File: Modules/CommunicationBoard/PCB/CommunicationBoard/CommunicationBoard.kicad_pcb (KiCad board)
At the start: 2 copper layers, 50 x 60 mm, 12 parts, among them J1 CIO_MAIN_CONNECTOR, J2 Conn_Coaxial, U1 SX1278

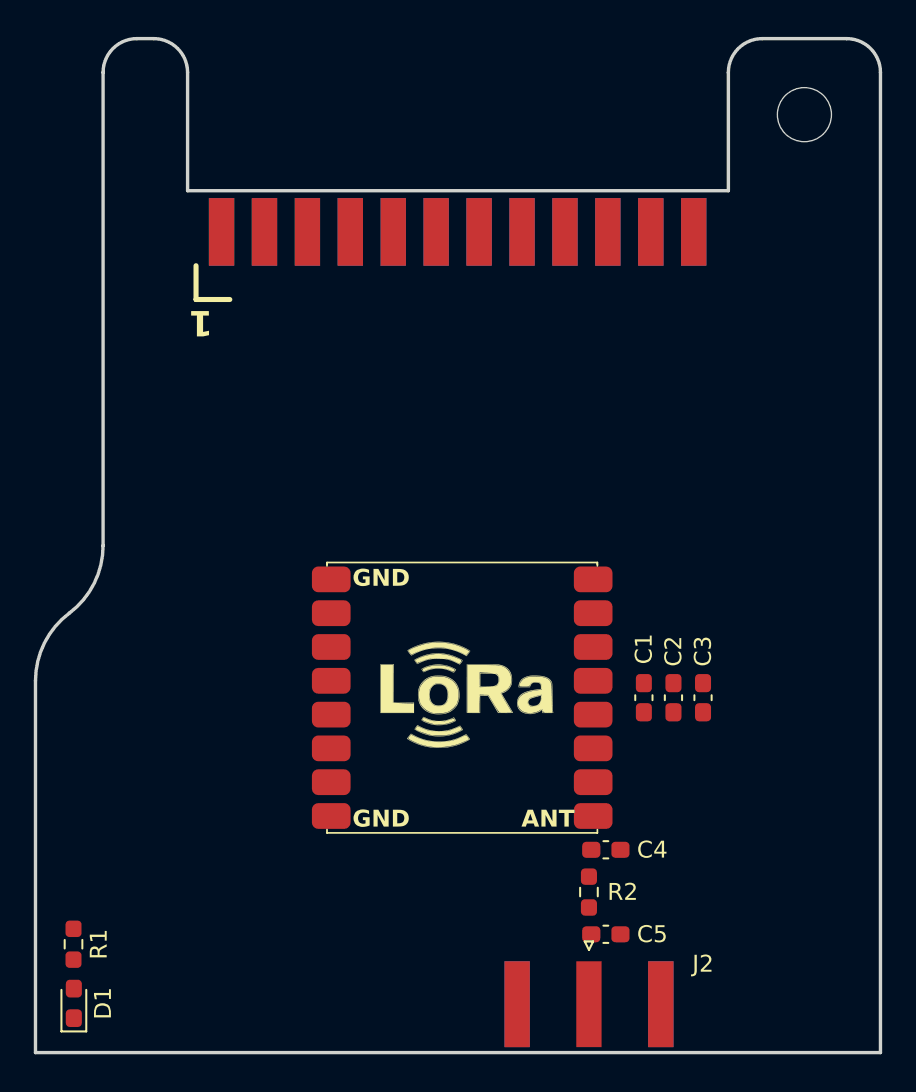
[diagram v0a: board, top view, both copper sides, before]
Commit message: Update Communication Board with E22-900M30S module
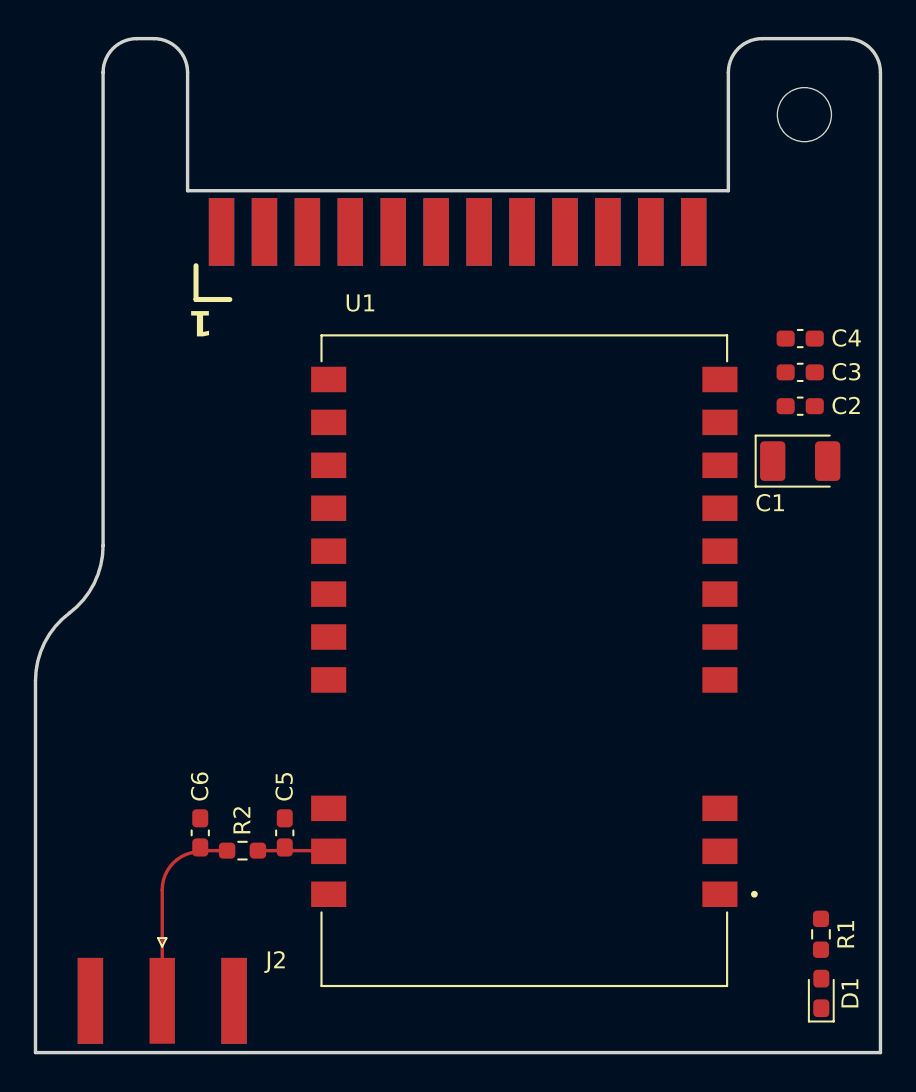
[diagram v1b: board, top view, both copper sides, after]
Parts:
- added C6: NC, Capacitor_SMD:C_0603_1608Metric_Pad1.08x0.95mm_HandSolder, F.Cu at (134.8, 112.0)
- C1: value 10uF -> 220u; footprint Capacitor_SMD:C_0603_1608Metric_Pad1.08x0.95mm_HandSolder -> Capacitor_Tantalum_SMD:CP_EIA-3528-21_Kemet-B_Pad1.50x2.35mm_HandSolder
- C2: value 0.1uF -> 10uF
- C4: value NC -> 0.1uF
- U1: value SX1278 -> E22-900M30S; footprint IcaroFootprints:SX1278 MODULE -> IcaroFootprints:XCVR_E22-900M30S
- moved D1 44.2 mm to (171.5, 121.5)
- moved R1 44.2 mm to (171.5, 118.0)
- moved C4 32.4 mm to (170.2, 82.8)
- moved J2 25.3 mm to (132.5, 121.9)
- moved R2 20.6 mm to (137.2, 113.0), turned to 180 degrees
- moved C3 20.1 mm to (170.2, 84.8), turned to 0 degrees
- moved C5 19.9 mm to (139.8, 112.0), turned to 90 degrees
- moved C2 18.8 mm to (170.2, 86.8), turned to 0 degrees
- moved C1 16.8 mm to (170.2, 90.0), turned to 0 degrees
- moved U1 4.28 mm to (153.9, 101.8)
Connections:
- C4 pad 1: Net-(U1-ANT) -> +3.3V
- C5 pad 1: Net-(J2-In) -> Net-(U1-ANT)
- U1 pad 10: GND -> +3.3V
- U1 pad 11: unconnected-(U1-DIO3-Pad11) -> GND
- U1 pad 12: unconnected-(U1-DIO4-Pad12) -> GND
- U1 pad 13: +3.3V -> unconnected-(U1-DIO1-Pad13)
- U1 pad 16: unconnected-(U1-DIO2-Pad16) -> /SPI.MOSI
- U1 pad 2: /SPI.MISO -> GND
- U1 pad 3: /SPI.MOSI -> GND
- U1 pad 4: /SPI.SCK -> GND
- U1 pad 5: unconnected-(U1-NSS-Pad5) -> GND
- U1 pad 8: GND -> unconnected-(U1-DIO2-Pad8)
- U1 pad 9: Net-(U1-ANT) -> +3.3V
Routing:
- net Net-(J2-In): track 0.00 -> 11.9 mm
- net Net-(U1-ANT): track 0.00 -> 4.20 mm

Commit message: First PCB layout version
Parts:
- added JP1: SolderJumper_2_Bridged, Jumper:SolderJumper-2_P1.3mm_Bridged_RoundedPad1.0x1.5mm, B.Cu at (147.3, 88.2)
- added JP2: SolderJumper_2_Bridged, Jumper:SolderJumper-2_P1.3mm_Bridged_RoundedPad1.0x1.5mm, B.Cu at (150.8, 88.2)
- added JP3: SolderJumper_2_Bridged, Jumper:SolderJumper-2_P1.3mm_Bridged_RoundedPad1.0x1.5mm, B.Cu at (154.4, 88.2)
- added JP4: SolderJumper_2_Bridged, Jumper:SolderJumper-2_P1.3mm_Bridged_RoundedPad1.0x1.5mm, B.Cu at (157.9, 88.2)
- added TP1: TestPoint, TestPoint:TestPoint_Pad_D2.5mm, F.Cu at (136.2, 87.5)
- added TP2: TestPoint, TestPoint:TestPoint_Pad_D2.5mm, F.Cu at (136.2, 92.5)
- added kibuzzard-67F40C11: G***, kibuzzard-67F40C11, F.Cu at (132.2, 87.6)
- added kibuzzard-67F40C24: G***, kibuzzard-67F40C24, F.Cu at (132.3, 92.6)
- added kibuzzard-67F40C7C: G***, kibuzzard-67F40C7C, B.Cu at (147.3, 92.1)
- added kibuzzard-67F40C92: G***, kibuzzard-67F40C92, B.Cu at (150.8, 92.1)
- added kibuzzard-67F40CAD: G***, kibuzzard-67F40CAD, B.Cu at (154.4, 92.1)
- added kibuzzard-67F40CB8: G***, kibuzzard-67F40CB8, B.Cu at (157.9, 92.1)
- added kibuzzard-67F40CCD: G***, kibuzzard-67F40CCD, F.Cu at (170.0, 119.4)
- moved C5 0.10 mm to (139.8, 112.1)
- moved C6 0.10 mm to (134.8, 112.1)
- moved J2 0.10 mm to (132.5, 122.0)
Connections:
- J1 pad 11: unconnected-(J1-IO0-Pad11) -> /IO0
- J1 pad 12: unconnected-(J1-IO1-Pad12) -> /IO1
- J1 pad 13: unconnected-(J1-IO2-Pad13) -> /IO2
- J1 pad 14: unconnected-(J1-IO3-Pad14) -> /IO3
- U1 pad 13: unconnected-(U1-DIO1-Pad13) -> /DIO1
- U1 pad 14: unconnected-(U1-BUSY-Pad14) -> /BUSY
- U1 pad 15: unconnected-(U1-~{RST}-Pad15) -> /~{RST}
- U1 pad 6: unconnected-(U1-RXEN-Pad6) -> /RXEN
- U1 pad 7: unconnected-(U1-TXEN-Pad7) -> /TXEN
- U1 pad 8: unconnected-(U1-DIO2-Pad8) -> /DIO2
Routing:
- net +3.3V: track 0.00 -> 64.2 mm, vias 0 -> 4
- net /DIO2: track 0.00 -> 45.5 mm
- net /SPI.CS0: track 0.00 -> 37.1 mm, vias 0 -> 1
- net /SPI.SCK: track 0.00 -> 34.3 mm, vias 0 -> 1
- net /SPI.MISO: track 0.00 -> 32.3 mm, vias 0 -> 1
- net /SPI.MOSI: track 0.00 -> 30.3 mm, vias 0 -> 1
- net /RXEN: track 0.00 -> 17.1 mm, vias 0 -> 1
- net /IO3: track 0.00 -> 13.9 mm, vias 0 -> 2
- net /IO2: track 0.00 -> 12.4 mm, vias 0 -> 1
- net /TXEN: track 0.00 -> 12.2 mm, vias 0 -> 1
- net /IO1: track 0.00 -> 12.0 mm, vias 0 -> 2
- net /IO0: track 0.00 -> 11.7 mm, vias 0 -> 1
- net /BUSY: track 0.00 -> 9.89 mm, vias 0 -> 1
- net /~{RST}: track 0.00 -> 8.89 mm, vias 0 -> 1
- net /DIO1: track 0.00 -> 6.19 mm
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- added copper zone on F.Cu, net +3.3V
- added copper zone on B.Cu, net GND
- added copper zone on F.Cu, net GND

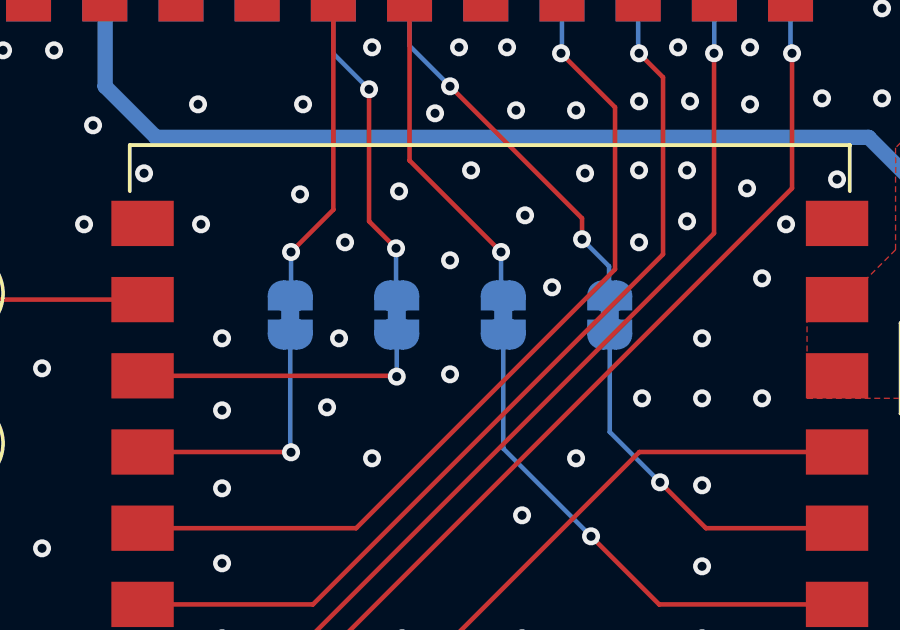
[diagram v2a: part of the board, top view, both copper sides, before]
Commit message: Change solder jumper from close to open
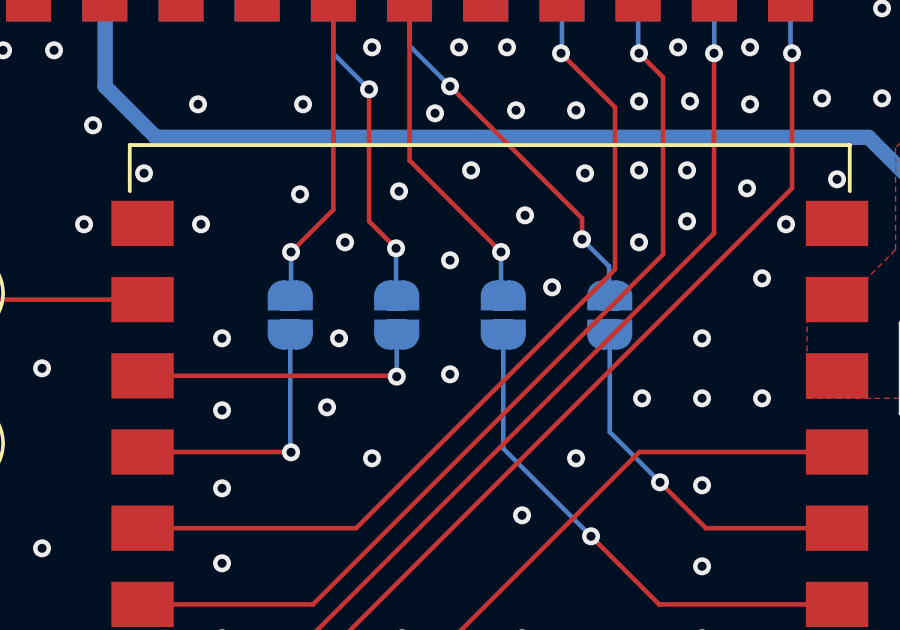
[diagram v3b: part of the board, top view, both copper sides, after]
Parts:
- JP1, JP2, JP3, JP4: value SolderJumper_2_Bridged -> SolderJumper_2_Open; footprint Jumper:SolderJumper-2_P1.3mm_Bridged_RoundedPad1.0x1.5mm -> Jumper:SolderJumper-2_P1.3mm_Open_RoundedPad1.0x1.5mm
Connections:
- J1 pad 23: /SPI.CS1 -> unconnected-(J1-CS1-Pad23)
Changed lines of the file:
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@@
 	(net 27 "/DIO1")
 	(net 28 "/DIO2")
-	(net 29 "/SPI.CS1")
+	(net 29 "unconnected-(J1-CS1-Pad23)")
 	(footprint "LED_SMD:LED_0603_1608Metric_Pad1.05x0.95mm_HandSolder"
 		(layer "F.Cu")
@@
 				(font
 					(size 0.001 0.001)
+					(thickness 0.15)
 				)
 			)
@@
 				(font
 					(size 0.001 0.001)
+					(thickness 0.15)
 				)
 			)
@@
 				(font
 					(size 0.001 0.001)
+					(thickness 0.15)
 				)
 			)
@@
 				(font
 					(size 0.001 0.001)
+					(thickness 0.15)
 				)
 			)
@@
 			(size 1.5 4)
 			(layers "F.Cu" "F.Mask" "F.Paste")
-			(net 29 "/SPI.CS1")
+			(net 29 "unconnected-(J1-CS1-Pad23)")
 			(pinfunction "CS1")
-			(pintype "bidirectional")
+			(pintype "bidirectional+no_connect")
 			(thermal_bridge_angle 45)
 		)
@@
 				(font
 					(size 0.001 0.001)
+					(thickness 0.15)
 				)
 			)
@@
 				(font
 					(size 0.001 0.001)
+					(thickness 0.15)
 				)
 			)
@@
 				(font
 					(size 0.001 0.001)
+					(thickness 0.15)
 				)
 				(justify mirror)
@@
 				(font
 					(size 0.001 0.001)
+					(thickness 0.15)
 				)
 				(justify mirror)
@@
 				(font
 					(size 0.001 0.001)
+					(thickness 0.15)
 				)
 				(justify mirror)
@@
 				(font
 					(size 0.001 0.001)
+					(thickness 0.15)
 				)
 				(justify mirror)
@@
 		(embedded_fonts no)
 	)
-	(footprint "Jumper:SolderJumper-2_P1.3mm_Bridged_RoundedPad1.0x1.5mm"
+	(footprint "Jumper:SolderJumper-2_P1.3mm_Open_RoundedPad1.0x1.5mm"
 		(layer "B.Cu")
 		(at 157.92325 88.22325 -90)
-		(descr "SMD Solder Jumper, 1x1.5mm, rounded Pads, 0.3mm gap, bridged with 1 copper strip")
-		(tags "net tie solder jumper bridged")
+		(descr "SMD Solder Jumper, 1x1.5mm, rounded Pads, 0.3mm gap, open")
+		(tags "solder jumper open")
 		(property "Reference" "JP4"
-			(at -2.32325 0.02325 180)
+			(at -2.42325 0.02325 180)
 			(layer "B.SilkS")
 			(effects
@@
 			)
 		)
-		(property "Value" "SolderJumper_2_Bridged"
+		(property "Value" "SolderJumper_2_Open"
 			(at 0 -1.9 90)
 			(layer "B.Fab")
@@
 			)
 		)
-		(property "Description" "Solder Jumper, 2-pole, closed/bridged"
+		(property "Description" "Solder Jumper, 2-pole, open"
 			(at 0 0 90)
 			(unlocked yes)
@@
 			)
 		)
-		(property ki_fp_filters "SolderJumper*Bridged*")
+		(property ki_fp_filters "SolderJumper*Open*")
 		(sheetname "/")
 		(sheetfile "CommunicationBoard.kicad_sch")
 		(zone_connect 1)
 		(attr exclude_from_pos_files exclude_from_bom allow_soldermask_bridges)
-		(net_tie_pad_groups "1, 2")
-		(fp_poly
-			(pts
-				(xy 0.25 0.3) (xy -0.25 0.3) (xy -0.25 -0.3) (xy 0.25 -0.3)
-			)
-			(stroke
-				(width 0)
-				(type solid)
-			)
-			(fill yes)
-			(layer "B.Cu")
-		)
 		(fp_rect
 			(start -0.15 0.75)
@@
 		(embedded_fonts no)
 	)
-	(footprint "Jumper:SolderJumper-2_P1.3mm_Bridged_RoundedPad1.0x1.5mm"
+	(footprint "Jumper:SolderJumper-2_P1.3mm_Open_RoundedPad1.0x1.5mm"
 		(layer "B.Cu")
 		(at 150.82325 88.22325 -90)
-		(descr "SMD Solder Jumper, 1x1.5mm, rounded Pads, 0.3mm gap, bridged with 1 copper strip")
-		(tags "net tie solder jumper bridged")
+		(descr "SMD Solder Jumper, 1x1.5mm, rounded Pads, 0.3mm gap, open")
+		(tags "solder jumper open")
 		(property "Reference" "JP2"
-			(at -2.42325 0 180)
+			(at -2.42325 -0.07675 180)
 			(layer "B.SilkS")
 			(effects
@@
 			)
 		)
-		(property "Value" "SolderJumper_2_Bridged"
+		(property "Value" "SolderJumper_2_Open"
 			(at 0 -1.9 90)
 			(layer "B.Fab")
@@
 			)
 		)
-		(property "Description" "Solder Jumper, 2-pole, closed/bridged"
+		(property "Description" "Solder Jumper, 2-pole, open"
 			(at 0 0 90)
 			(unlocked yes)
@@
 			)
 		)
-		(property ki_fp_filters "SolderJumper*Bridged*")
+		(property ki_fp_filters "SolderJumper*Open*")
 		(sheetname "/")
 		(sheetfile "CommunicationBoard.kicad_sch")
 		(zone_connect 1)
 		(attr exclude_from_pos_files exclude_from_bom allow_soldermask_bridges)
-		(net_tie_pad_groups "1, 2")
-		(fp_poly
-			(pts
-				(xy 0.25 0.3) (xy -0.25 0.3) (xy -0.25 -0.3) (xy 0.25 -0.3)
-			)
-			(stroke
-				(width 0)
-				(type solid)
-			)
-			(fill yes)
-			(layer "B.Cu")
-		)
 		(fp_rect
 			(start -0.15 0.75)
@@
 				(font
 					(size 0.001 0.001)
+					(thickness 0.15)
 				)
 				(justify mirror)
@@
 				(font
 					(size 0.001 0.001)
+					(thickness 0.15)
 				)
 				(justify mirror)
@@
 		(embedded_fonts no)
 	)
-	(footprint "Jumper:SolderJumper-2_P1.3mm_Bridged_RoundedPad1.0x1.5mm"
+	(footprint "Jumper:SolderJumper-2_P1.3mm_Open_RoundedPad1.0x1.5mm"
 		(layer "B.Cu")
 		(at 154.37325 88.22325 -90)
-		(descr "SMD Solder Jumper, 1x1.5mm, rounded Pads, 0.3mm gap, bridged with 1 copper strip")
-		(tags "net tie solder jumper bridged")
+		(descr "SMD Solder Jumper, 1x1.5mm, rounded Pads, 0.3mm gap, open")
+		(tags "solder jumper open")
 		(property "Reference" "JP3"
-			(at -2.32325 -0.02675 180)
+			(at -2.42325 -0.02675 180)
 			(layer "B.SilkS")
 			(effects
@@
 			)
 		)
-		(property "Value" "SolderJumper_2_Bridged"
+		(property "Value" "SolderJumper_2_Open"
 			(at 0 -1.9 90)
 			(layer "B.Fab")
@@
 			)
 		)
-		(property "Description" "Solder Jumper, 2-pole, closed/bridged"
+		(property "Description" "Solder Jumper, 2-pole, open"
 			(at 0 0 90)
 			(unlocked yes)
@@
 			)
 		)
-		(property ki_fp_filters "SolderJumper*Bridged*")
+		(property ki_fp_filters "SolderJumper*Open*")
 		(sheetname "/")
 		(sheetfile "CommunicationBoard.kicad_sch")
 		(zone_connect 1)
 		(attr exclude_from_pos_files exclude_from_bom allow_soldermask_bridges)
-		(net_tie_pad_groups "1, 2")
-		(fp_poly
-			(pts
-				(xy 0.25 0.3) (xy -0.25 0.3) (xy -0.25 -0.3) (xy 0.25 -0.3)
-			)
-			(stroke
-				(width 0)
-				(type solid)
-			)
-			(fill yes)
-			(layer "B.Cu")
-		)
 		(fp_rect
 			(start -0.15 0.75)
@@
 				(font
 					(size 0.001 0.001)
+					(thickness 0.15)
 				)
 				(justify mirror)
@@
 				(font
 					(size 0.001 0.001)
+					(thickness 0.15)
 				)
 				(justify mirror)
@@
 		(embedded_fonts no)
 	)
-	(footprint "Jumper:SolderJumper-2_P1.3mm_Bridged_RoundedPad1.0x1.5mm"
+	(footprint "Jumper:SolderJumper-2_P1.3mm_Open_RoundedPad1.0x1.5mm"
 		(layer "B.Cu")
 		(at 147.27325 88.22325 -90)
-		(descr "SMD Solder Jumper, 1x1.5mm, rounded Pads, 0.3mm gap, bridged with 1 copper strip")
-		(tags "net tie solder jumper bridged")
+		(descr "SMD Solder Jumper, 1x1.5mm, rounded Pads, 0.3mm gap, open")
+		(tags "solder jumper open")
 		(property "Reference" "JP1"
 			(at -2.42325 -0.02675 180)
@@
 			)
 		)
-		(property "Value" "SolderJumper_2_Bridged"
+		(property "Value" "SolderJumper_2_Open"
 			(at 0 -1.9 90)
 			(layer "B.Fab")
@@
 			)
 		)
-		(property "Description" "Solder Jumper, 2-pole, closed/bridged"
+		(property "Description" "Solder Jumper, 2-pole, open"
 			(at 0 0 90)
 			(unlocked yes)
@@
 			)
 		)
-		(property ki_fp_filters "SolderJumper*Bridged*")
+		(property ki_fp_filters "SolderJumper*Open*")
 		(sheetname "/")
 		(sheetfile "CommunicationBoard.kicad_sch")
 		(zone_connect 1)
 		(attr exclude_from_pos_files exclude_from_bom allow_soldermask_bridges)
-		(net_tie_pad_groups "1, 2")
-		(fp_poly
-			(pts
-				(xy 0.25 0.3) (xy -0.25 0.3) (xy -0.25 -0.3) (xy 0.25 -0.3)
-			)
-			(stroke
-				(width 0)
-				(type solid)
-			)
-			(fill yes)
-			(layer "B.Cu")
-		)
 		(fp_rect
 			(start -0.15 0.75)
@@
 		(polygon
 			(pts
-				(xy 125 125) (xy 175 125) (xy 175 74) (xy 175 74) (xy 175 74) (xy 175 74.5) (xy 129 74.5) (xy 129 96)
-				(xy 129 95.75) (xy 125 99.75)
+				(xy 125 125) (xy 175 125) (xy 175 74) (xy 175 74.5) (xy 129 74.5) (xy 129 96) (xy 129 95.75) (xy 125 99.75)
 			)
 		)
